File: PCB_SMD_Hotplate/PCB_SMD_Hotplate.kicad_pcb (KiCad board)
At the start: 2 copper layers, 90 x 60 mm, 4 parts

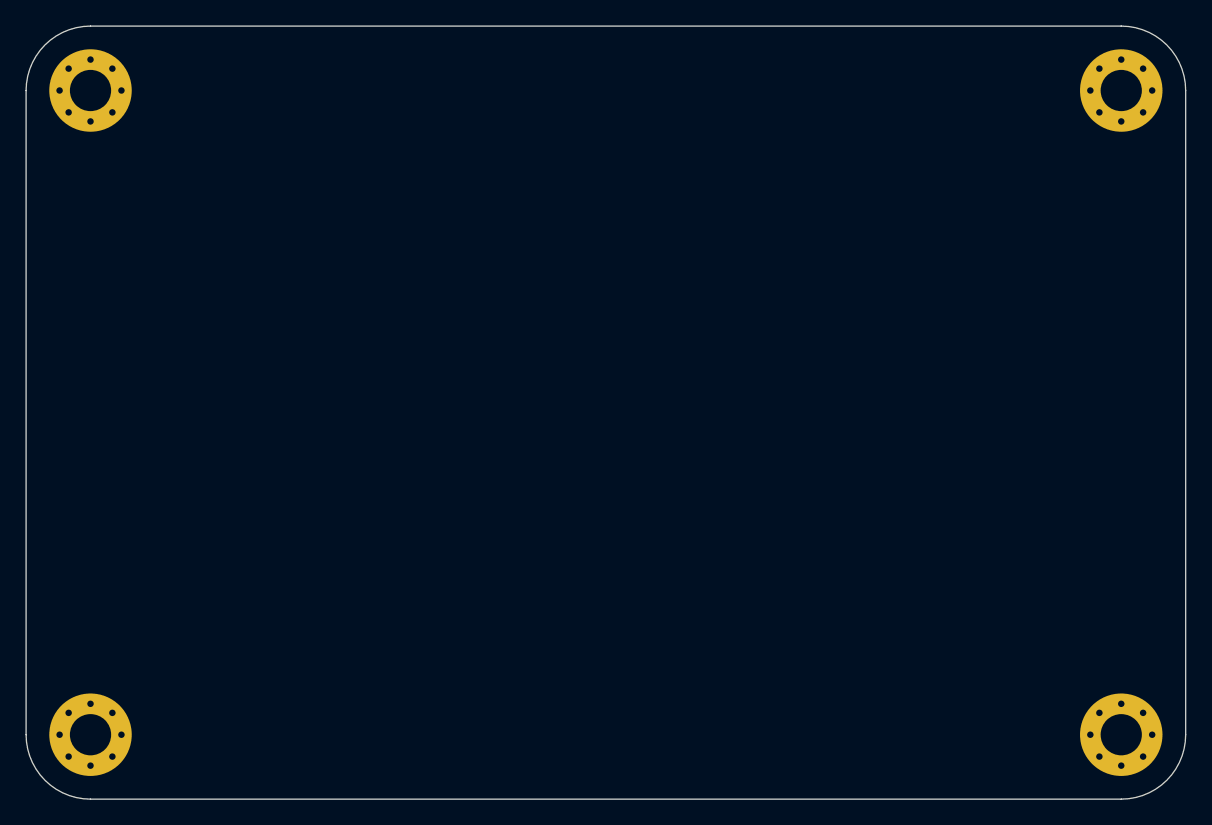
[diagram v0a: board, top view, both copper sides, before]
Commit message: Finish schm, finish component layout
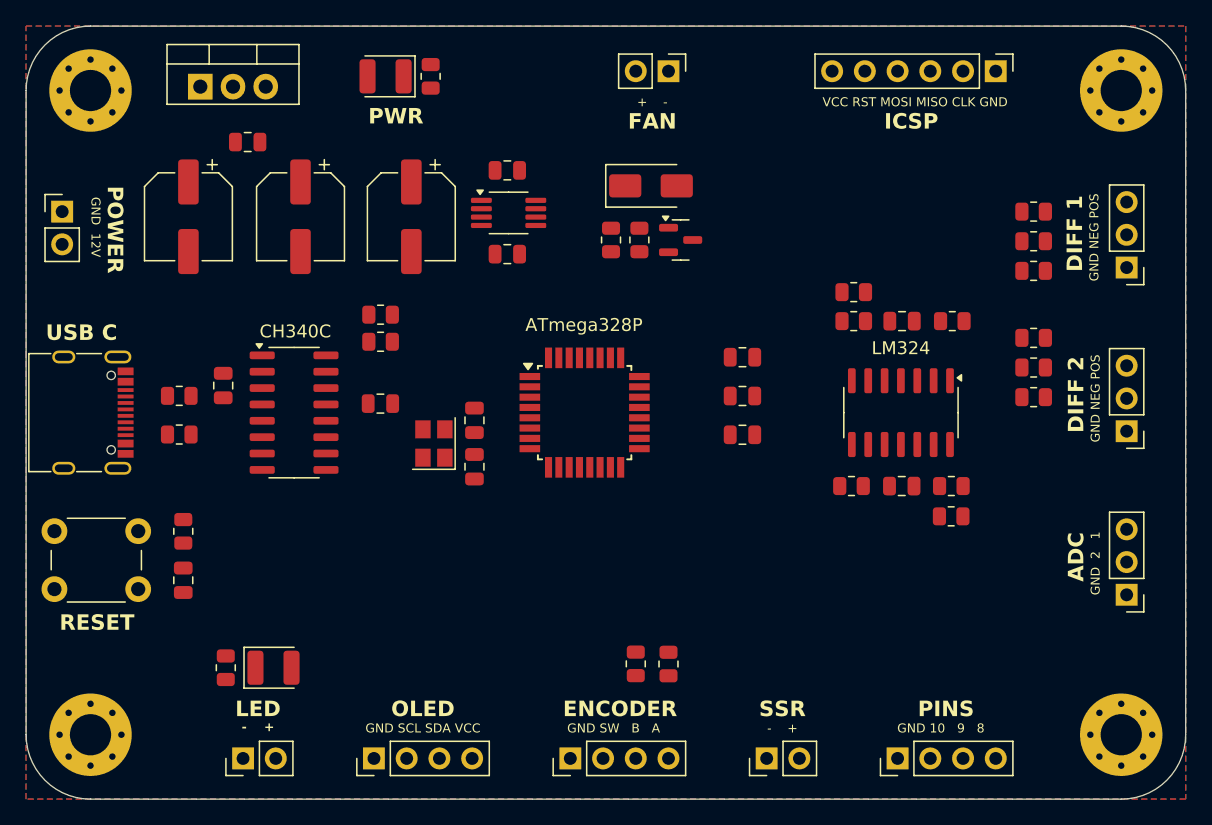
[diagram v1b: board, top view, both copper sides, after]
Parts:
- added C1: 100n, Capacitor_SMD:C_0805_2012Metric, F.Cu at (115.3, 87.9)
- added C10: 100n, Capacitor_SMD:C_0805_2012Metric, F.Cu at (155.6, 85.7)
- added C11: 100n, Capacitor_SMD:C_0805_2012Metric, F.Cu at (155.6, 88.7)
- added C12: 100n, Capacitor_SMD:C_0805_2012Metric, F.Cu at (155.6, 91.7)
- added C13: 100n, Capacitor_SMD:C_0805_2012Metric, F.Cu at (168.0, 82.9)
- added C14: 10p, Capacitor_SMD:C_0805_2012Metric, F.Cu at (134.8, 94.2)
- added C15: 100n, Capacitor_SMD:C_0805_2012Metric, F.Cu at (168.0, 95.7)
- added C16: 100n, Capacitor_SMD:C_0805_2012Metric, F.Cu at (112.2, 103.0)
- added C2: 10u, Capacitor_SMD:CP_Elec_6.3x7.7, F.Cu at (112.6, 74.8)
- added C3: 1u, Capacitor_SMD:C_0805_2012Metric, F.Cu at (117.2, 69.0)
- added C4: 10u, Capacitor_SMD:CP_Elec_6.3x7.7, F.Cu at (121.3, 74.8)
- added C5: 100n, Capacitor_SMD:C_0805_2012Metric, F.Cu at (127.5, 89.3)
- added C6: 1u, Capacitor_SMD:C_0805_2012Metric, F.Cu at (137.3, 71.2)
- added C7: 1u, Capacitor_SMD:C_0805_2012Metric, F.Cu at (137.3, 77.7)
- added C8: 10u, Capacitor_SMD:CP_Elec_6.3x7.7, F.Cu at (129.9, 74.8)
- added C9: 10p, Capacitor_SMD:C_0805_2012Metric, F.Cu at (134.8, 90.6)
- added D1: SS14, Diode_SMD:D_SMA, F.Cu at (148.5, 72.4)
- added D2: RED, LED_SMD:LED_1210_3225Metric, F.Cu at (127.9, 63.9)
- added D3: GREEN, LED_SMD:LED_1210_3225Metric, F.Cu at (119.2, 109.8)
- added J1: CONN_POWER, Connector_PinHeader_2.54mm:PinHeader_1x02_P2.54mm_Vertical, F.Cu at (102.8, 74.4)
- added J10: CONN_DIFF_01, Connector_PinHeader_2.54mm:PinHeader_1x03_P2.54mm_Vertical, F.Cu at (185.4, 78.7)
- added J11: CONN_DIFF_02, Connector_PinHeader_2.54mm:PinHeader_1x03_P2.54mm_Vertical, F.Cu at (185.4, 91.4)
- added J12: CONN_HEADER, Connector_PinHeader_2.54mm:PinHeader_1x04_P2.54mm_Vertical, F.Cu at (167.6, 116.8)
- added J2: USB_C_16P, Connector_USB:USB_C_Receptacle_G-Switch_GT-USB-7010ASV, F.Cu at (104.0, 90.0)
- added J3: CONN_ADC, Connector_PinHeader_2.54mm:PinHeader_1x03_P2.54mm_Vertical, F.Cu at (185.4, 104.1)
- added J4: CONN_OLED, Connector_PinHeader_2.54mm:PinHeader_1x04_P2.54mm_Vertical, F.Cu at (127.0, 116.8)
- added J5: CONN_FAN, Connector_PinHeader_2.54mm:PinHeader_1x02_P2.54mm_Vertical, F.Cu at (149.9, 63.5)
- added J6: CONN_LED, Connector_PinHeader_2.54mm:PinHeader_1x02_P2.54mm_Vertical, F.Cu at (116.8, 116.8)
- added J7: CONN_ENCODER, Connector_PinHeader_2.54mm:PinHeader_1x04_P2.54mm_Vertical, F.Cu at (142.2, 116.8)
- added J8: CONN_SSR, Connector_PinHeader_2.54mm:PinHeader_1x02_P2.54mm_Vertical, F.Cu at (157.5, 116.8)
- added J9: CONN_ICSP, Connector_PinHeader_2.54mm:PinHeader_1x06_P2.54mm_Vertical, F.Cu at (175.3, 63.5)
- added Q1: 2N7002, Package_TO_SOT_SMD:SOT-23, F.Cu at (150.8, 76.6)
- added R1: 5k1, Resistor_SMD:R_0805_2012Metric, F.Cu at (111.9, 88.7)
- added R10: 4k7, Resistor_SMD:R_0805_2012Metric, F.Cu at (115.5, 109.8)
- added R11: 10k, Resistor_SMD:R_0805_2012Metric, F.Cu at (112.2, 99.2)
- added R12: 47k, Resistor_SMD:R_0805_2012Metric, F.Cu at (178.2, 74.4)
- added R13: 1k, Resistor_SMD:R_0805_2012Metric, F.Cu at (178.2, 76.7)
- added R14: 1k, Resistor_SMD:R_0805_2012Metric, F.Cu at (178.2, 79.0)
- added R15: 47k, Resistor_SMD:R_0805_2012Metric, F.Cu at (171.9, 82.9)
- added R16: 1k, Resistor_SMD:R_0805_2012Metric, F.Cu at (164.2, 80.7)
- added R17: 100k, Resistor_SMD:R_0805_2012Metric, F.Cu at (164.2, 82.9)
- added R18: 47k, Resistor_SMD:R_0805_2012Metric, F.Cu at (178.2, 84.2)
- added R19: 1k, Resistor_SMD:R_0805_2012Metric, F.Cu at (178.2, 86.5)
- added R2: 1k, Resistor_SMD:R_0805_2012Metric, F.Cu at (127.5, 82.4)
- added R20: 1k, Resistor_SMD:R_0805_2012Metric, F.Cu at (178.2, 88.8)
- added R21: 47k, Resistor_SMD:R_0805_2012Metric, F.Cu at (164.1, 95.7)
- added R22: 1k, Resistor_SMD:R_0805_2012Metric, F.Cu at (171.8, 98.0)
- added R23: 100k, Resistor_SMD:R_0805_2012Metric, F.Cu at (171.8, 95.7)
- added R3: 5k1, Resistor_SMD:R_0805_2012Metric, F.Cu at (111.9, 91.7)
- added R4: 1k, Resistor_SMD:R_0805_2012Metric, F.Cu at (127.5, 84.5)
- added R5: 4k7, Resistor_SMD:R_0805_2012Metric, F.Cu at (131.4, 63.9)
- added R6: 4k7, Resistor_SMD:R_0805_2012Metric, F.Cu at (145.4, 76.6)
- added R7: 10k, Resistor_SMD:R_0805_2012Metric, F.Cu at (147.6, 76.6)
- added R8: 10k, Resistor_SMD:R_0805_2012Metric, F.Cu at (147.3, 109.5)
- added R9: 10k, Resistor_SMD:R_0805_2012Metric, F.Cu at (149.9, 109.5)
- added SW1: SW_Push, Button_Switch_THT:SW_PUSH_6mm_H4.3mm, F.Cu at (102.2, 99.2)
- added U1: LM7805_TO220, Package_TO_SOT_THT:TO-220-3_Vertical, F.Cu at (113.5, 64.7)
- added U2: CH340C, Package_SO:SOIC-16_3.9x9.9mm_P1.27mm, F.Cu at (120.8, 90.0)
- added U3: ICL7660, Package_SO:MSOP-8_3x3mm_P0.65mm, F.Cu at (137.4, 74.5)
- added U4: LM324, Package_SO:SOIC-14_3.9x8.7mm_P1.27mm, F.Cu at (167.9, 90.0)
- added U5: ATmega328P-A, Package_QFP:TQFP-32_7x7mm_P0.8mm, F.Cu at (143.3, 90.0)
- added Y1: 16MHz, Crystal:Crystal_SMD_3225-4Pin_3.2x2.5mm, F.Cu at (131.7, 92.4)
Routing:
- added copper zone on B.Cu, net GND
- added copper zone on F.Cu, net GND
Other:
- board text added: "+ -"
- board text added: "- +"
- board text added: "ADC"
- board text added: "ATmega328P"
- board text added: "CH340C"
- board text added: "DIFF 1"
- board text added: "DIFF 2"
- board text added: "ENCODER"
- board text added: "FAN"
- board text added: "GND 10 9 8"
- board text added: "GND 12V"
- board text added: "GND 2 1"
- board text added: "GND NEG POS"
- board text added: "GND SCL SDA VCC"
- board text added: "GND SW B A"
- board text added: "ICSP"
- board text added: "LED"
- board text added: "LM324"
- board text added: "OLED"
- board text added: "PINS"
- board text added: "POWER"
- board text added: "PWR"
- board text added: "RESET"
- board text added: "SSR"
- board text added: "USB C"
- board text added: "VCC RST MOSI MISO CLK GND"

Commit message: Finish layout and routing
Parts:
- removed the C12 at (155.6, 91.7)
- moved C10 19.6 mm to (136.4, 89.8), turned to 90 degrees
- moved C11 5.60 mm to (150.4, 90.9), turned to 90 degrees
- moved D2 3.46 mm to (125.8, 66.7)
- moved R5 3.46 mm to (129.3, 66.7)
- moved C13 0.80 mm to (134.0, 94.2)
- moved C9 0.80 mm to (134.0, 90.6)
- moved Y1 0.80 mm to (130.8, 92.4)
- renumbered C13 to C12, C14 to C13, C15 to C14, C16 to C15
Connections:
- J12 pad 2: PIN_10_UC -> PIN_08_UC
- J12 pad 4: PIN_08_UC -> PIN_10_UC
- J9 pad 2: SPI_SCLK_UC -> SPI_MOSI_UC
- J9 pad 4: SPI_MOSI_UC -> SPI_SCLK_UC
- U5 pad 11: ENCODER_SW -> ENCODER_A
- U5 pad 9: ENCODER_A -> ENCODER_SW
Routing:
- net +5V: track 0.00 -> 277.6 mm, vias 0 -> 8
- net RST_UC: track 0.00 -> 89.7 mm, vias 0 -> 2
- net +12V: track 0.00 -> 65.3 mm
- net SPI_MOSI_UC: track 0.00 -> 48.9 mm
- net -5V: track 0.00 -> 44.7 mm, vias 0 -> 2
- net SPI_MISO_UC: track 0.00 -> 44.4 mm
- net ADC_IN_02: track 0.00 -> 43.8 mm, vias 0 -> 1
- net ADC_IN_01: track 0.00 -> 43.3 mm, vias 0 -> 1
- net PIN_10_UC: track 0.00 -> 42.2 mm
- net PIN_09_UC: track 0.00 -> 41.4 mm
- net PIN_08_UC: track 0.00 -> 40.6 mm
- net LED_OUT: track 0.00 -> 40.6 mm, vias 0 -> 2
- net SPI_SCLK_UC: track 0.00 -> 40.5 mm
- net SSR_UC: track 0.00 -> 39.4 mm, vias 0 -> 1
- net GND: track 0.00 -> 38.5 mm, vias 0 -> 31
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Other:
- board text added: "GND 8 9 10"
- board text added: "JLCJLCJLCJLC"
- board text added: "SMD Hotplate Controller"
- board text added: "VCC RST CLK MISO MOSI GND"
- board text added: "github.com/AleksaHeler/PCB_SMD_Hotplate"
- board text added: "v1.0"
- board text removed: "GND 10 9 8"
- board text removed: "VCC RST MOSI MISO CLK GND"

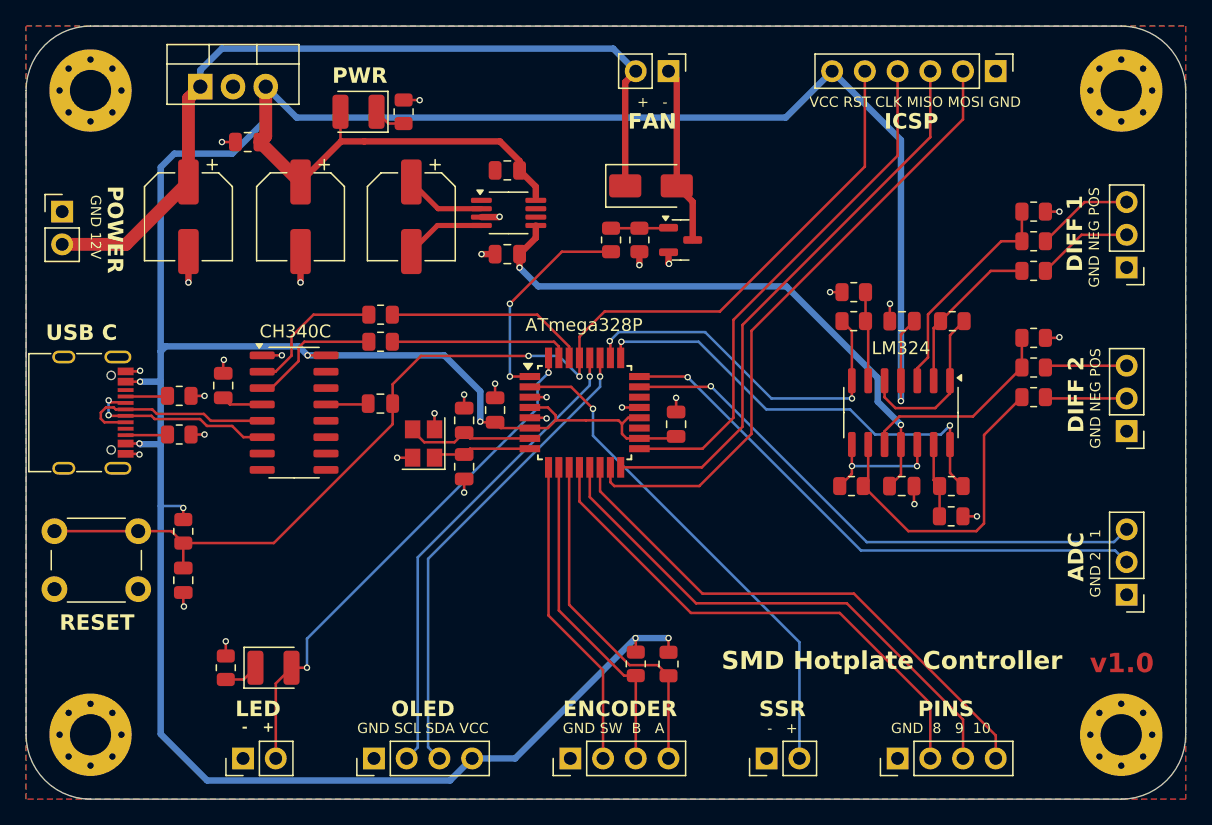
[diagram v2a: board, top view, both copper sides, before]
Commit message: Finish PCB and prepare files for ordering
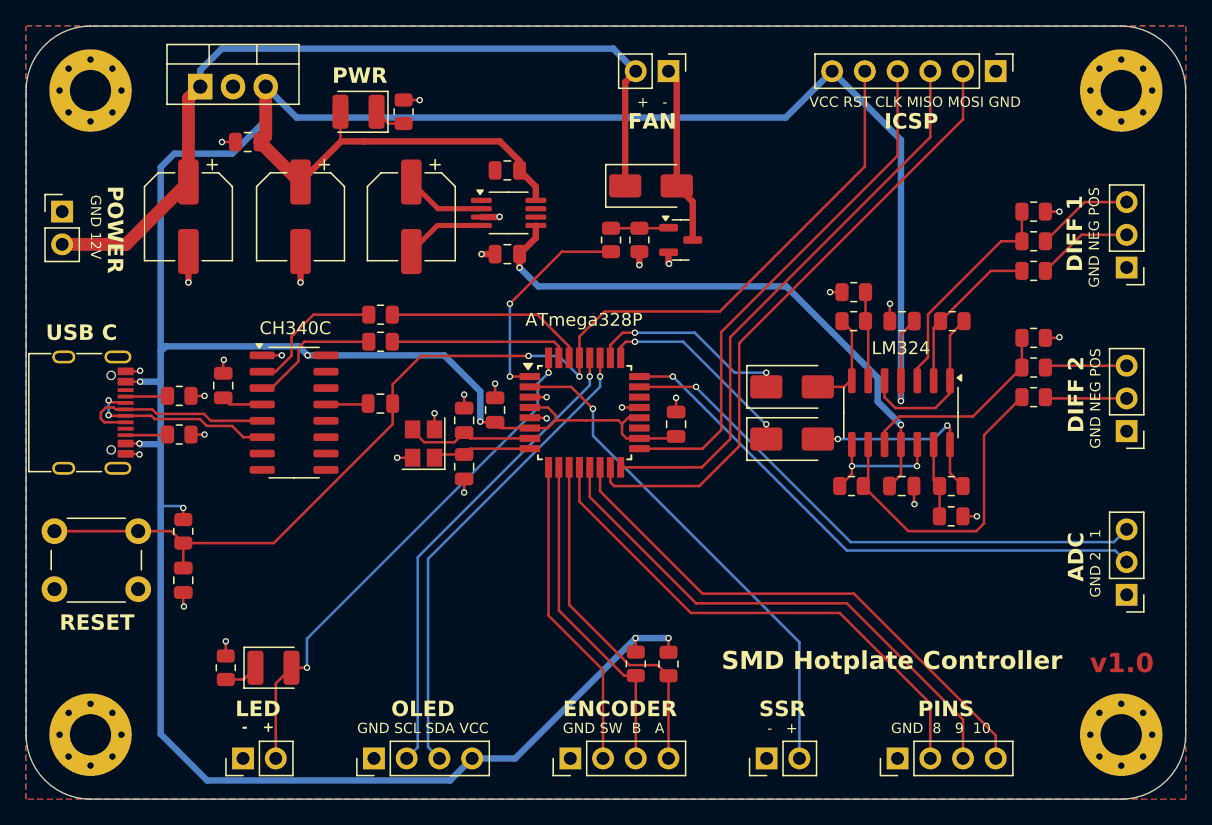
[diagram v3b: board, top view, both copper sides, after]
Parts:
- added D4: SS14, Diode_SMD:D_SMA, F.Cu at (159.4, 88.0)
- added D5: SS14, Diode_SMD:D_SMA, F.Cu at (159.4, 92.0)
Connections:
- R17 pad 1: DIFF_IN_01 -> Net-(D4-A)
- R23 pad 1: DIFF_IN_02 -> Net-(D5-A)
- U4 pad 14: DIFF_IN_02 -> Net-(D5-A)
- U4 pad 7: DIFF_IN_01 -> Net-(D4-A)
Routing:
- net DIFF_IN_02: track 35.2 -> 16.1 mm
- net Net-(D5-A): track 0.00 -> 15.7 mm, vias 0 -> 2
- net DIFF_IN_01: track 29.4 -> 16.4 mm
- net Net-(D4-A): track 0.00 -> 7.78 mm
